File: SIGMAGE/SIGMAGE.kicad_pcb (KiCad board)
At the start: 4 copper layers, 100 x 85 mm, 123 parts, among them J1 UJ31CHG2SMTTR, J10 TSW10607GS, J11 HTSW10807GD, J12 HTSW10807GD, J13 HTSW10807GD, J14 HTSW10807GD, J15 HTSW10807GD, J16 HTSW10807GD, J17 HTSW10807GD, J2 SJ63073E, J3 SJ63073E, J4 SJ63073E, J5 SJ63073E, J6 18407728, J7 TSW10607GS, J8 TSW10607GS, J9 TSW10607GS, U1 MAX8902BATA/V+T, U2 MAX8902BATA/V+T, U3 MAX8902BATA/V+T, U4 OPA1612AIDRGR, U5 PCM1803ADB, U6 OPA1612AIDRGR, U7 PCM1803ADB, U8 STM32F407VGTx, U9 LAN8720ACP, X1 STDCSU18M, X2 STDCSK425M

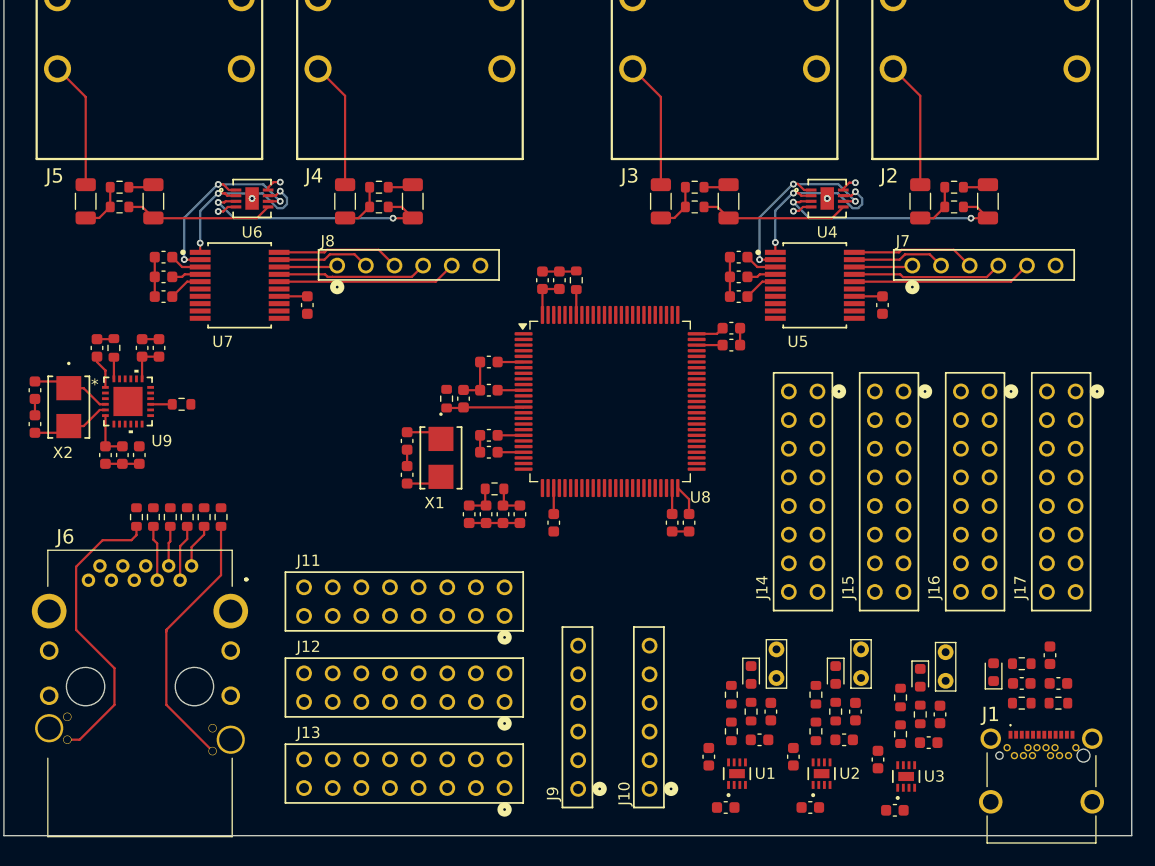
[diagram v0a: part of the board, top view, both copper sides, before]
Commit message: Almost finished routing
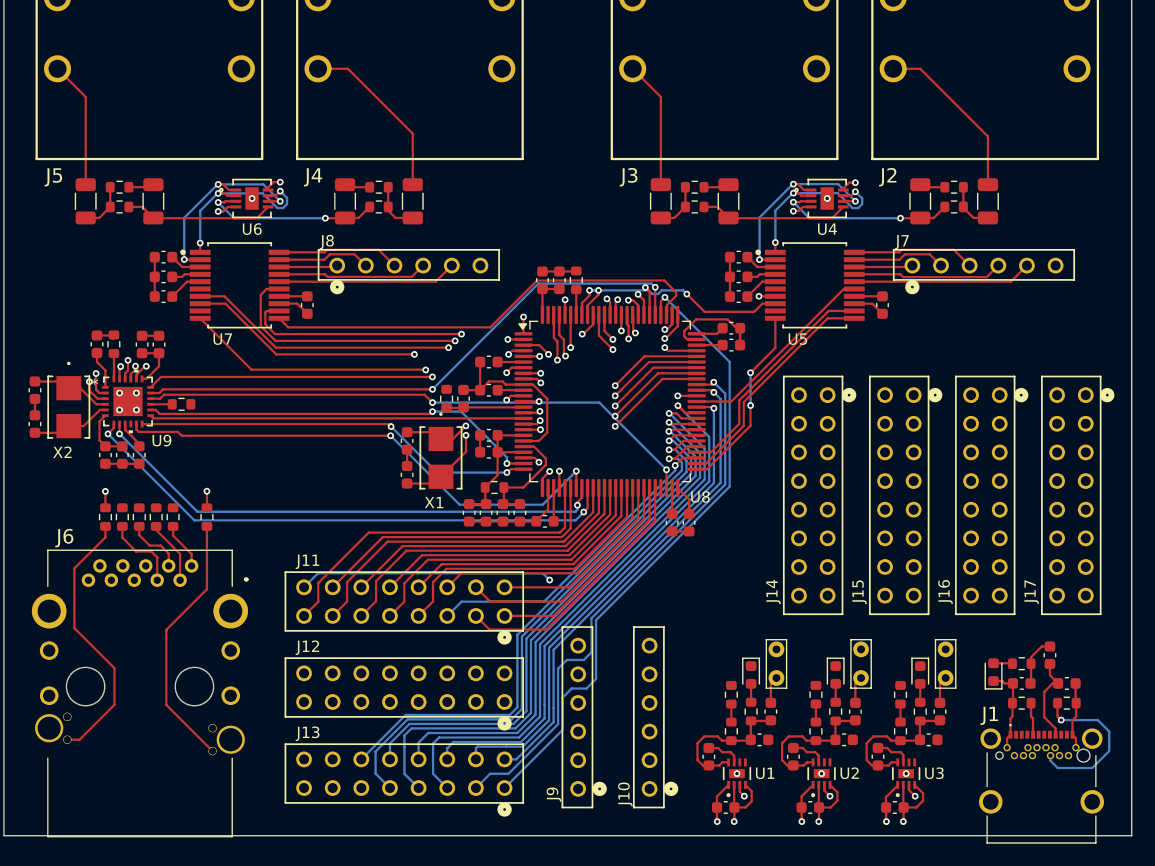
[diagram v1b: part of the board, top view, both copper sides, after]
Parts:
- moved C12 6.00 mm to (107.2, 49.8)
- moved C18 6.00 mm to (56.2, 49.8)
- moved C20 6.00 mm to (101.2, 49.8)
- moved C22 6.00 mm to (50.2, 49.8)
- moved R24 2.75 mm to (29.0, 77.8)
- moved R27 2.75 mm to (33.5, 77.8)
- moved R28 2.75 mm to (35.0, 77.8)
- moved R29 2.75 mm to (30.5, 77.8)
- moved R30 2.75 mm to (32.0, 77.8)
- moved R25 1.25 mm to (38.0, 77.8)
- moved J16 0.96 mm to (107.0, 75.8)
- moved J17 0.96 mm to (114.7, 75.8)
- moved J14 0.96 mm to (91.8, 75.8)
- moved J15 0.96 mm to (99.4, 75.8)
- moved C31 0.79 mm to (68.0, 78.1), turned to 180 degrees
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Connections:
- net Net-(U8-PE8) renamed GPIO_PE8
- J10 pad 1: JTMS_SWDIO -> JTRST
- J10 pad 2: JTCK_SWCLK -> JTDO_SWO
- J10 pad 4: JTDO_SWO -> JTCK_SWCLK
- J10 pad 5: JTRST -> JTMS_SWDIO
- J11 pad 1: Net-(U8-PE0) -> GPIO_PE14
- J11 pad 10: Net-(U8-PE9) -> GPIO_PE7
- J11 pad 11: Net-(U8-PE10) -> GPIO_PB2
- J11 pad 12: Net-(U8-PE11) -> GPIO_PB1
- J11 pad 13: Net-(U8-PE12) -> GPIO_PB0
- J11 pad 14: Net-(U8-PE13) -> GPIO_PA6
- J11 pad 15: Net-(U8-PE14) -> GPIO_PA5
- J11 pad 16: Net-(U8-PE15) -> GPIO_PA3
- J11 pad 2: Net-(U8-PE1) -> GPIO_PE12
- J11 pad 3: Net-(U8-PE2) -> GPIO_PE15
- J11 pad 4: Net-(U8-PE3) -> GPIO_PE13
- J11 pad 5: Net-(U8-PE4) -> GPIO_PB14
- J11 pad 6: Net-(U8-PE5) -> GPIO_PE11
- J11 pad 7: Net-(U8-PE6) -> GPIO_PE10
- J11 pad 8: Net-(U8-PE7) -> GPIO_PE9
- J12 pad 1: Net-(U8-PD0) -> GPIO_PC3
- J12 pad 10: Net-(U8-PD9) -> GPIO_PD5
- J12 pad 11: Net-(U8-PD10) -> GPIO_PE0
- J12 pad 12: Net-(U8-PD11) -> GPIO_PD7
- J12 pad 13: Net-(U8-PD12) -> GPIO_PE4
- J12 pad 14: Net-(U8-PD13) -> GPIO_PE1
- J12 pad 15: Net-(U8-PD14) -> GPIO_PE2
- J12 pad 16: Net-(U8-PD15) -> GPIO_PE3
- J12 pad 2: Net-(U8-PD1) -> GPIO_PA0
- J12 pad 3: Net-(U8-PD2) -> GPIO_PC0
- J12 pad 4: Net-(U8-PD3) -> GPIO_PC2
- J12 pad 5: Net-(U8-PD4) -> GPIO_PC14
- J12 pad 6: Net-(U8-PD5) -> GPIO_PC15
- J12 pad 7: Net-(U8-PD6) -> GPIO_PE5
- J12 pad 8: Net-(U8-PD7) -> GPIO_PE6
- J12 pad 9: Net-(U8-PD8) -> GPIO_PD6
- J13 pad 1: Net-(U8-PA0) -> GPIO_PC11
- J13 pad 10: Net-(U8-PC2) -> GPIO_PD10
- J13 pad 11: Net-(U8-PC3) -> GPIO_PD4
- J13 pad 12: Net-(U8-PC8) -> GPIO_PD8
- J13 pad 13: Net-(U8-PC9) -> GPIO_PD0
- J13 pad 14: Net-(U8-PC11) -> GPIO_PD3
- J13 pad 15: Net-(U8-PC14) -> GPIO_PD1
- J13 pad 16: Net-(U8-PC15) -> GPIO_PD2
- J13 pad 2: Net-(U8-PA3) -> GPIO_PC8
- J13 pad 3: Net-(U8-PA5) -> GPIO_PC9
- J13 pad 4: Net-(U8-PA6) -> GPIO_PD15
- J13 pad 5: Net-(U8-PB0) -> GPIO_PD13
- J13 pad 6: Net-(U8-PB1) -> GPIO_PD14
- J13 pad 7: Net-(U8-PB2) -> GPIO_PD11
- J13 pad 8: Net-(U8-PB14) -> GPIO_PD12
- J13 pad 9: Net-(U8-PC0) -> GPIO_PD9
- J9 pad 1: USART1_CTS -> USART1_CK
- J9 pad 2: USART1_RTS -> USART1_TX
- J9 pad 3: USART1_TX -> USART1_RX
- J9 pad 4: USART1_RX -> USART1_CTS
- J9 pad 5: USART1_CK -> USART1_RTS
- U8 pad 1: Net-(U8-PE2) -> GPIO_PE2
- U8 pad 15: Net-(U8-PC0) -> GPIO_PC0
- U8 pad 17: Net-(U8-PC2) -> GPIO_PC2
- U8 pad 18: Net-(U8-PC3) -> GPIO_PC3
- U8 pad 2: Net-(U8-PE3) -> GPIO_PE3
- U8 pad 23: Net-(U8-PA0) -> GPIO_PA0
- U8 pad 26: Net-(U8-PA3) -> GPIO_PA3
- U8 pad 3: Net-(U8-PE4) -> GPIO_PE4
- U8 pad 30: Net-(U8-PA5) -> GPIO_PA5
- U8 pad 31: Net-(U8-PA6) -> GPIO_PA6
- U8 pad 35: Net-(U8-PB0) -> GPIO_PB0
- U8 pad 36: Net-(U8-PB1) -> GPIO_PB1
- U8 pad 37: Net-(U8-PB2) -> GPIO_PB2
- U8 pad 38: Net-(U8-PE7) -> GPIO_PE7
- U8 pad 4: Net-(U8-PE5) -> GPIO_PE5
- U8 pad 40: Net-(U8-PE9) -> GPIO_PE9
- U8 pad 41: Net-(U8-PE10) -> GPIO_PE10
- U8 pad 42: Net-(U8-PE11) -> GPIO_PE11
- U8 pad 43: Net-(U8-PE12) -> GPIO_PE12
- U8 pad 44: Net-(U8-PE13) -> GPIO_PE13
- U8 pad 45: Net-(U8-PE14) -> GPIO_PE14
- U8 pad 46: Net-(U8-PE15) -> GPIO_PE15
- U8 pad 5: Net-(U8-PE6) -> GPIO_PE6
- U8 pad 53: Net-(U8-PB14) -> GPIO_PB14
- U8 pad 55: Net-(U8-PD8) -> GPIO_PD8
- U8 pad 56: Net-(U8-PD9) -> GPIO_PD9
- U8 pad 57: Net-(U8-PD10) -> GPIO_PD10
- U8 pad 58: Net-(U8-PD11) -> GPIO_PD11
- U8 pad 59: Net-(U8-PD12) -> GPIO_PD12
- U8 pad 60: Net-(U8-PD13) -> GPIO_PD13
- U8 pad 61: Net-(U8-PD14) -> GPIO_PD14
- U8 pad 62: Net-(U8-PD15) -> GPIO_PD15
- U8 pad 65: Net-(U8-PC8) -> GPIO_PC8
- U8 pad 66: Net-(U8-PC9) -> GPIO_PC9
- U8 pad 79: Net-(U8-PC11) -> GPIO_PC11
- U8 pad 8: Net-(U8-PC14) -> GPIO_PC14
- U8 pad 81: Net-(U8-PD0) -> GPIO_PD0
- U8 pad 82: Net-(U8-PD1) -> GPIO_PD1
- U8 pad 83: Net-(U8-PD2) -> GPIO_PD2
- U8 pad 84: Net-(U8-PD3) -> GPIO_PD3
- U8 pad 85: Net-(U8-PD4) -> GPIO_PD4
- U8 pad 86: Net-(U8-PD5) -> GPIO_PD5
- U8 pad 87: Net-(U8-PD6) -> GPIO_PD6
- U8 pad 88: Net-(U8-PD7) -> GPIO_PD7
- U8 pad 9: Net-(U8-PC15) -> GPIO_PC15
- U8 pad 97: Net-(U8-PE0) -> GPIO_PE0
- U8 pad 98: Net-(U8-PE1) -> GPIO_PE1
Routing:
- net GPIO_PD0: track 0.00 -> 78.9 mm, vias 0 -> 1
- net GPIO_PD4: track 0.00 -> 73.5 mm, vias 0 -> 1
- net GPIO_PD1: track 0.00 -> 72.1 mm, vias 0 -> 1
- net GPIO_PD3: track 0.00 -> 70.3 mm, vias 0 -> 1
- net GPIO_PD2: track 0.00 -> 67.8 mm, vias 0 -> 1
- net GND: track 35.4 -> 101.2 mm, vias 4 -> 14
- net GPIO_PC11: track 0.00 -> 56.6 mm, vias 0 -> 1
- net GPIO_PD6: track 0.00 -> 52.4 mm, vias 0 -> 1
- net GPIO_PD13: track 0.00 -> 51.8 mm, vias 0 -> 1
- net GPIO_PD11: track 0.00 -> 51.8 mm, vias 0 -> 1
- net GPIO_PE0: track 0.00 -> 51.5 mm, vias 0 -> 1
- net PHY_TXD0: track 0.00 -> 51.3 mm, vias 0 -> 2
- net GPIO_PD9: track 0.00 -> 51.1 mm, vias 0 -> 1
- net PHY_TXEN: track 0.00 -> 50.3 mm, vias 0 -> 2
- net GPIO_PD7: track 0.00 -> 50.0 mm, vias 0 -> 1
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- added copper zone on In3.Cu, net +5V
- added copper zone on In3.Cu, net VBUS
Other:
- copper layers 4 -> 6

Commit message: Finished PCB
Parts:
- JP1, JP2, JP3: value Jumper_2_Open -> Jumper_2_Bridged; footprint TestPoint:TestPoint_Bridge_Pitch2.54mm_Drill0.7mm -> Panelization:MouseBite-Slot-Jumper_0201
- moved JP1 0.57 mm to (88.0, 91.8), turned to 180 degrees
- moved JP2 0.57 mm to (95.5, 91.8), turned to 180 degrees
- moved JP3 0.57 mm to (103.0, 91.8), turned to 180 degrees
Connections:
- FB1 pad 2: +3V3 -> Net-(JP1-A)
- FB2 pad 2: +2V5 -> Net-(JP2-A)
- FB3 pad 2: +1V2 -> Net-(JP3-A)
- JP1 pad 1: +3V3 -> Net-(JP1-A)
- JP2 pad 1: +2V5 -> Net-(JP2-A)
- JP3 pad 1: +1V2 -> Net-(JP3-A)
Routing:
- net +5V: track 28.0 -> 120.6 mm, vias 8 -> 12
- net PHY_NRST: track 1.92 -> 51.4 mm, vias 0 -> 2
- net GND: track 101.2 -> 148.5 mm, vias 14 -> 46
- net +3V3: track 47.3 -> 68.3 mm, vias 0 -> 18
- net VBUS: track 7.92 -> 15.8 mm, vias 0 -> 2
- net +2V5: track 11.5 -> 18.0 mm, vias 0 -> 5
- net Net-(U2-FB): track 1.60 -> 7.54 mm, vias 0 -> 2
- net Net-(U1-FB): track 1.60 -> 7.48 mm, vias 0 -> 2
- net Net-(U3-FB): track 1.60 -> 7.40 mm, vias 0 -> 2
- net GPIO_PA3: track 33.9 -> 37.7 mm
- net Net-(JP3-A): track 0.00 -> 2.16 mm
- net Net-(JP2-A): track 0.00 -> 2.16 mm
- net Net-(JP1-A): track 0.00 -> 2.16 mm
- net PHY_CRS_DV: track 45.0 -> 43.3 mm
- net ADC1_SCKI: track 18.1 -> 19.2 mm
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- added copper zone on In3.Cu, net +1V2
- added copper zone on In3.Cu, net +2V5
- added copper zone on In3.Cu, net +3V3

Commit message: Passed DRC check
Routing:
- net +5V: track 120.6 -> 122.0 mm

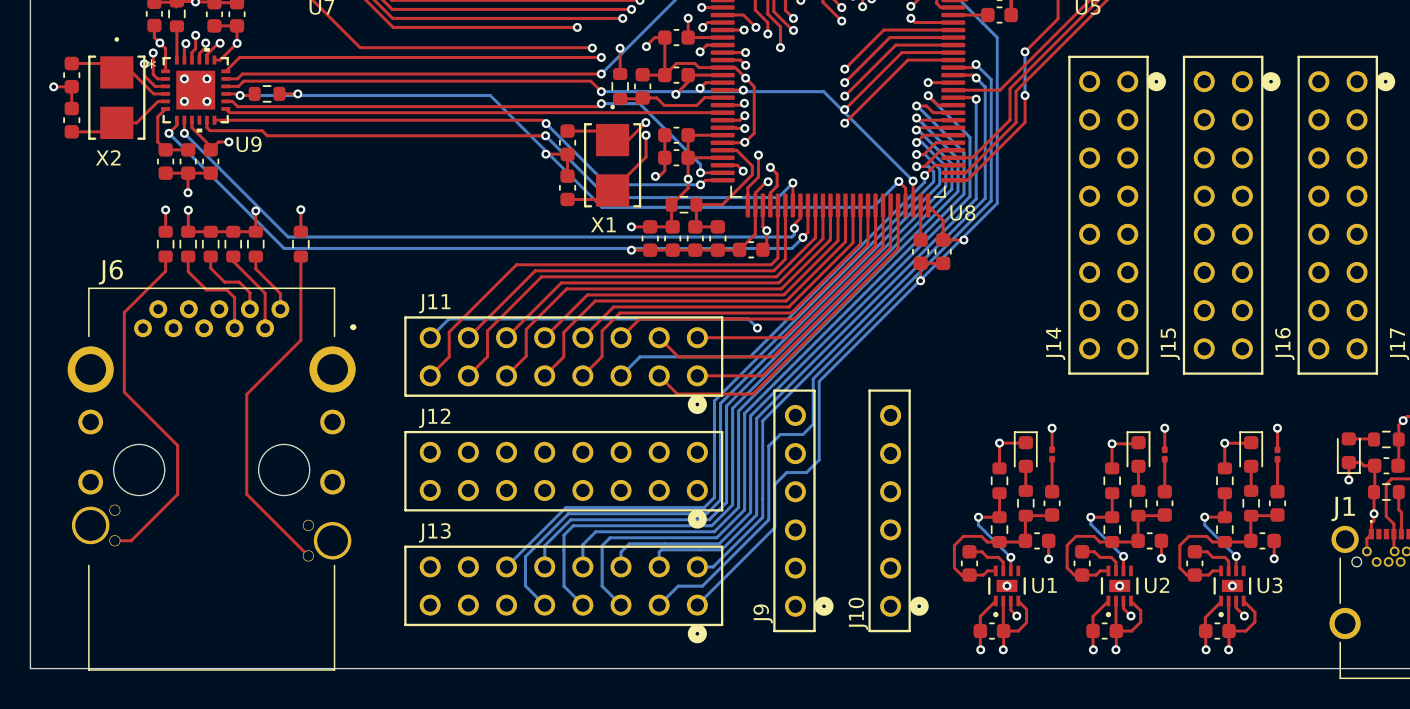
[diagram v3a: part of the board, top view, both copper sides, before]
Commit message: Final touches, PCB layout is still horrible, will fix in MK II
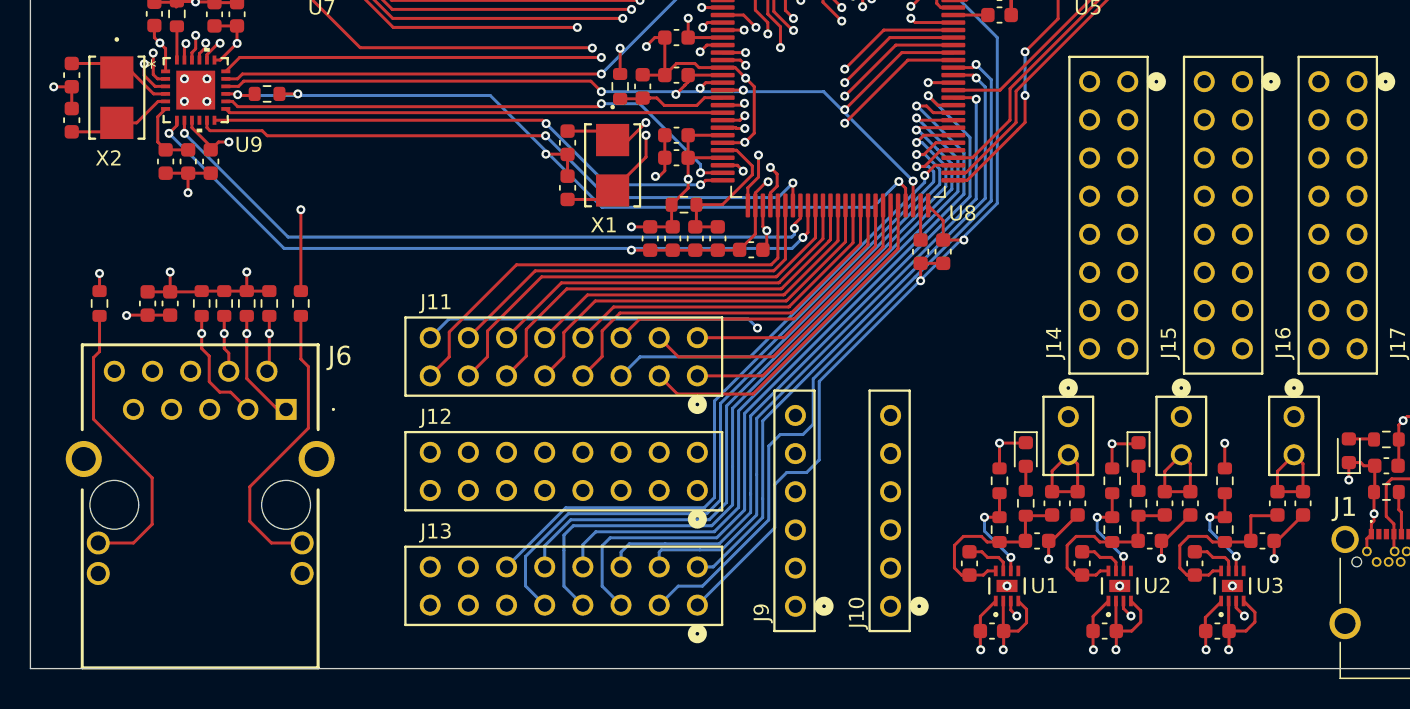
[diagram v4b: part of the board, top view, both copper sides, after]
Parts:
- removed D3: LED, LED_SMD:LED_0603_1608Metric
- removed JP1, JP2, JP3: Jumper_2_Bridged, Panelization:MouseBite-Slot-Jumper_0201
- removed R9: 300, Resistor_SMD:R_0603_1608Metric
- added C54: 100n, Capacitor_SMD:C_0603_1608Metric, F.Cu at (27.8, 81.7)
- added C55: 100n, Capacitor_SMD:C_0603_1608Metric, F.Cu at (29.3, 81.7)
- added C56: 1u, Capacitor_SMD:C_0603_1608Metric, F.Cu at (89.7, 95.0)
- added C57: 1u, Capacitor_SMD:C_0603_1608Metric, F.Cu at (97.2, 95.0)
- added C58: 1u, Capacitor_SMD:C_0603_1608Metric, F.Cu at (104.7, 95.0)
- added J18: HTSW10107GD, SIGMAGE:HTSW10107GD, F.Cu at (89.1, 90.5)
- added J19: HTSW10107GD, SIGMAGE:HTSW10107GD, F.Cu at (96.6, 90.5)
- added J20: HTSW10107GD, SIGMAGE:HTSW10107GD, F.Cu at (104.1, 90.5)
- FB1, FB2, FB3, FB4: value 600R 500mA -> 500 @ 100 MHz
- J6: value 18407728 -> ARJM11D7502ABEW2; footprint SIGMAGE:18407728 -> SIGMAGE:ARJM11D7502ABEW2
- R12: value 1k25 -> 300
- R3: value 825 -> 130
- R6: value 625 -> 50
- moved R24 5.91 mm to (24.6, 81.7)
- moved J6 5.58 mm to (37.0, 88.8)
- moved R27 4.05 mm to (34.4, 81.7)
- moved R28 4.05 mm to (35.9, 81.7)
- moved R29 4.05 mm to (31.4, 81.7)
- moved R30 4.05 mm to (32.9, 81.7)
- moved R25 3.95 mm to (38.0, 81.7)
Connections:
- J6 pad 10: GND -> unconnected-(J6-TD4--Pad10)
- J6 pad 11: Net-(J6-ANODE_YELLOW) -> Net-(J6-A_GREEN)
- J6 pad 13: Net-(J6-ANODE_GREEN) -> Net-(J6-A_YELLOW)
- J6 pad 5: unconnected-(J6-TRD3+-Pad5) -> +3V3
- J6 pad 6: unconnected-(J6-TRD3--Pad6) -> +3V3
- J6 pad 9: +3V3 -> unconnected-(J6-TD4+-Pad9)
- R24 pad 1: Net-(J6-ANODE_GREEN) -> Net-(J6-A_GREEN)
- R25 pad 1: Net-(J6-ANODE_YELLOW) -> Net-(J6-A_YELLOW)
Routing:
- net Net-(J6-ANODE_GREEN): track 23.9 -> 0.00 mm
- net Net-(J6-ANODE_YELLOW): track 23.1 -> 0.00 mm
- net Net-(J6-A_GREEN): track 0.00 -> 19.8 mm
- net Net-(J6-A_YELLOW): track 0.00 -> 19.6 mm
- net GND: track 148.7 -> 157.8 mm, vias 46 -> 47
- net Net-(C56-Pad1): track 2.16 -> 7.31 mm
- net Net-(C58-Pad1): track 2.16 -> 7.31 mm
- net Net-(C57-Pad1): track 2.16 -> 7.31 mm
- net Net-(U9-LED1/*REGOFF): track 14.3 -> 18.9 mm
- net Net-(J6-TD2-): track 30.6 -> 26.2 mm, vias 1 -> 2
- net Net-(U9-LED2/*NINTSEL): track 19.2 -> 23.2 mm
- net Net-(J6-TD1-): track 30.8 -> 33.2 mm, vias 1 -> 2
- net +3V3: track 68.1 -> 70.1 mm, vias 18 -> 17
- net Net-(D3-A): track 1.64 -> 0.00 mm
- net +2V5: track 18.0 -> 16.5 mm, vias 5 -> 4
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
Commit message: Again some touches against DigiKey's assortment
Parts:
- added R32: 200k, Resistor_SMD:R_0603_1608Metric, F.Cu at (92.0, 90.2)
- added R9: 270k, Resistor_SMD:R_0603_1608Metric, F.Cu at (84.5, 90.2)
- R2: value 540k -> 270k
- R5: value 380k -> 180k
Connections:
- R2 pad 2: GND -> Net-(R2-Pad2)
- R5 pad 2: GND -> Net-(R32-Pad1)
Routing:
- net Net-(R32-Pad1): track 0.00 -> 1.66 mm
- net Net-(R2-Pad2): track 0.00 -> 1.65 mm
